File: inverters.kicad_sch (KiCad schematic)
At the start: 10 parts, among them U13 74LVC1G04, U14 74LVC1G04, U15 74LVC1G04

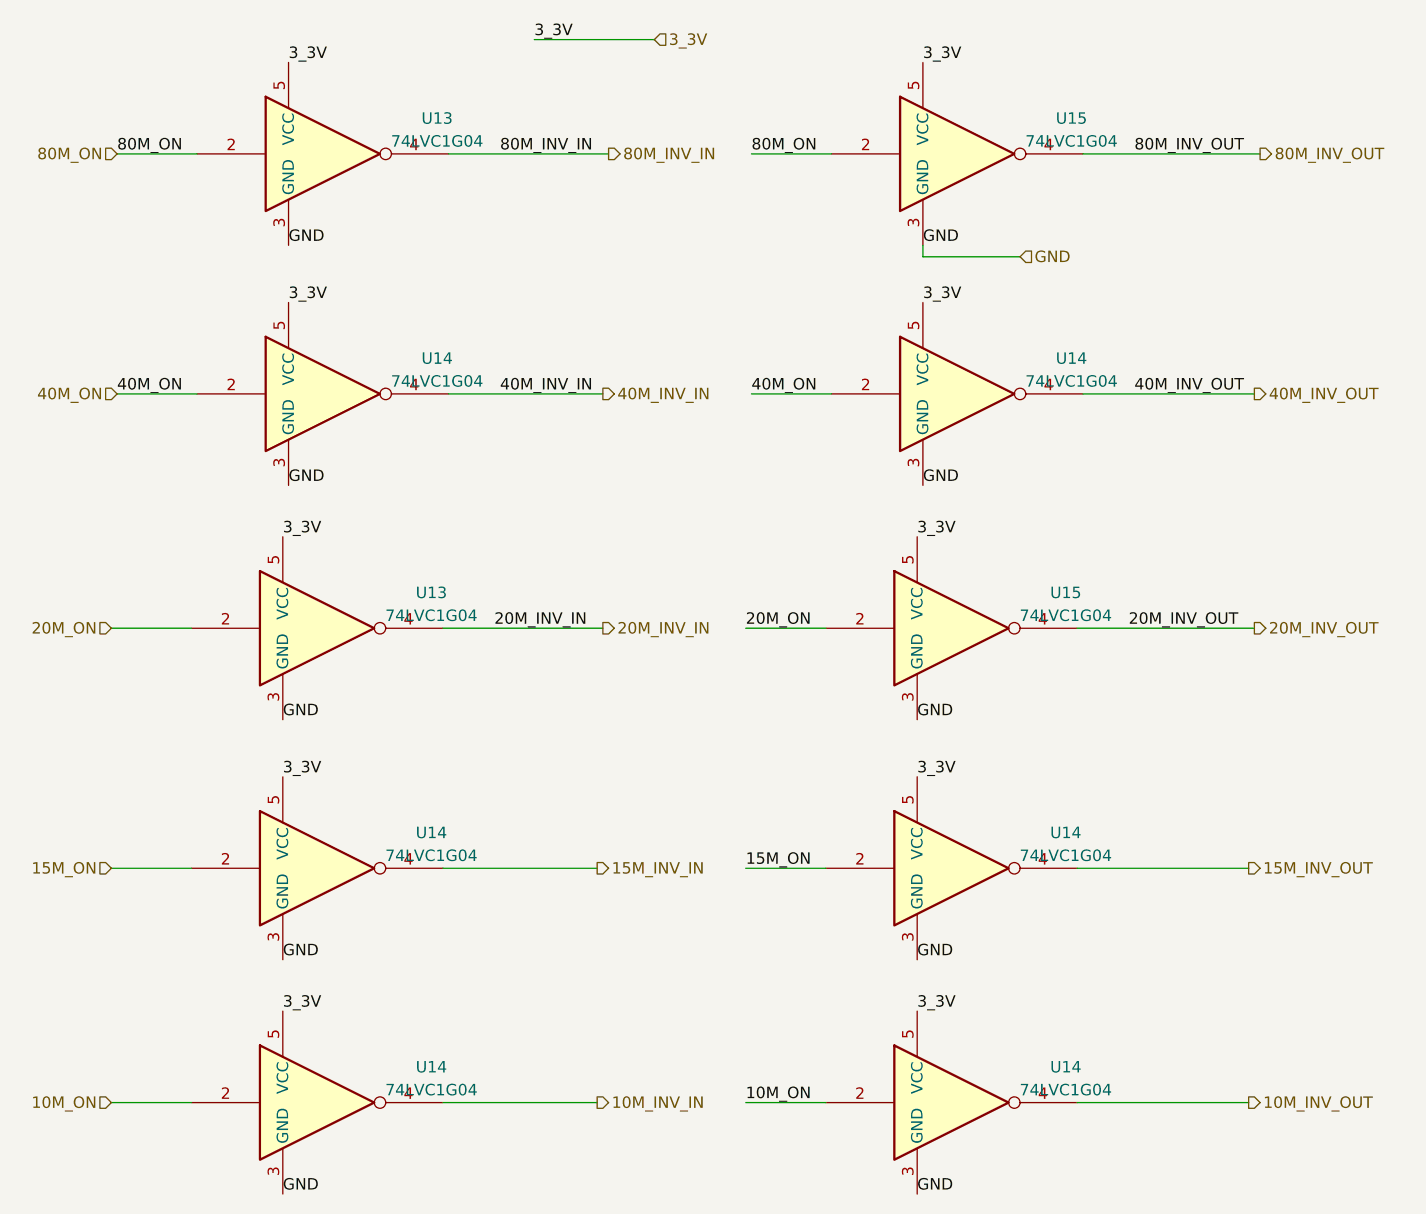
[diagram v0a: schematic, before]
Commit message: Fixed logic gate, is now NOR.  Cleaned up layout.
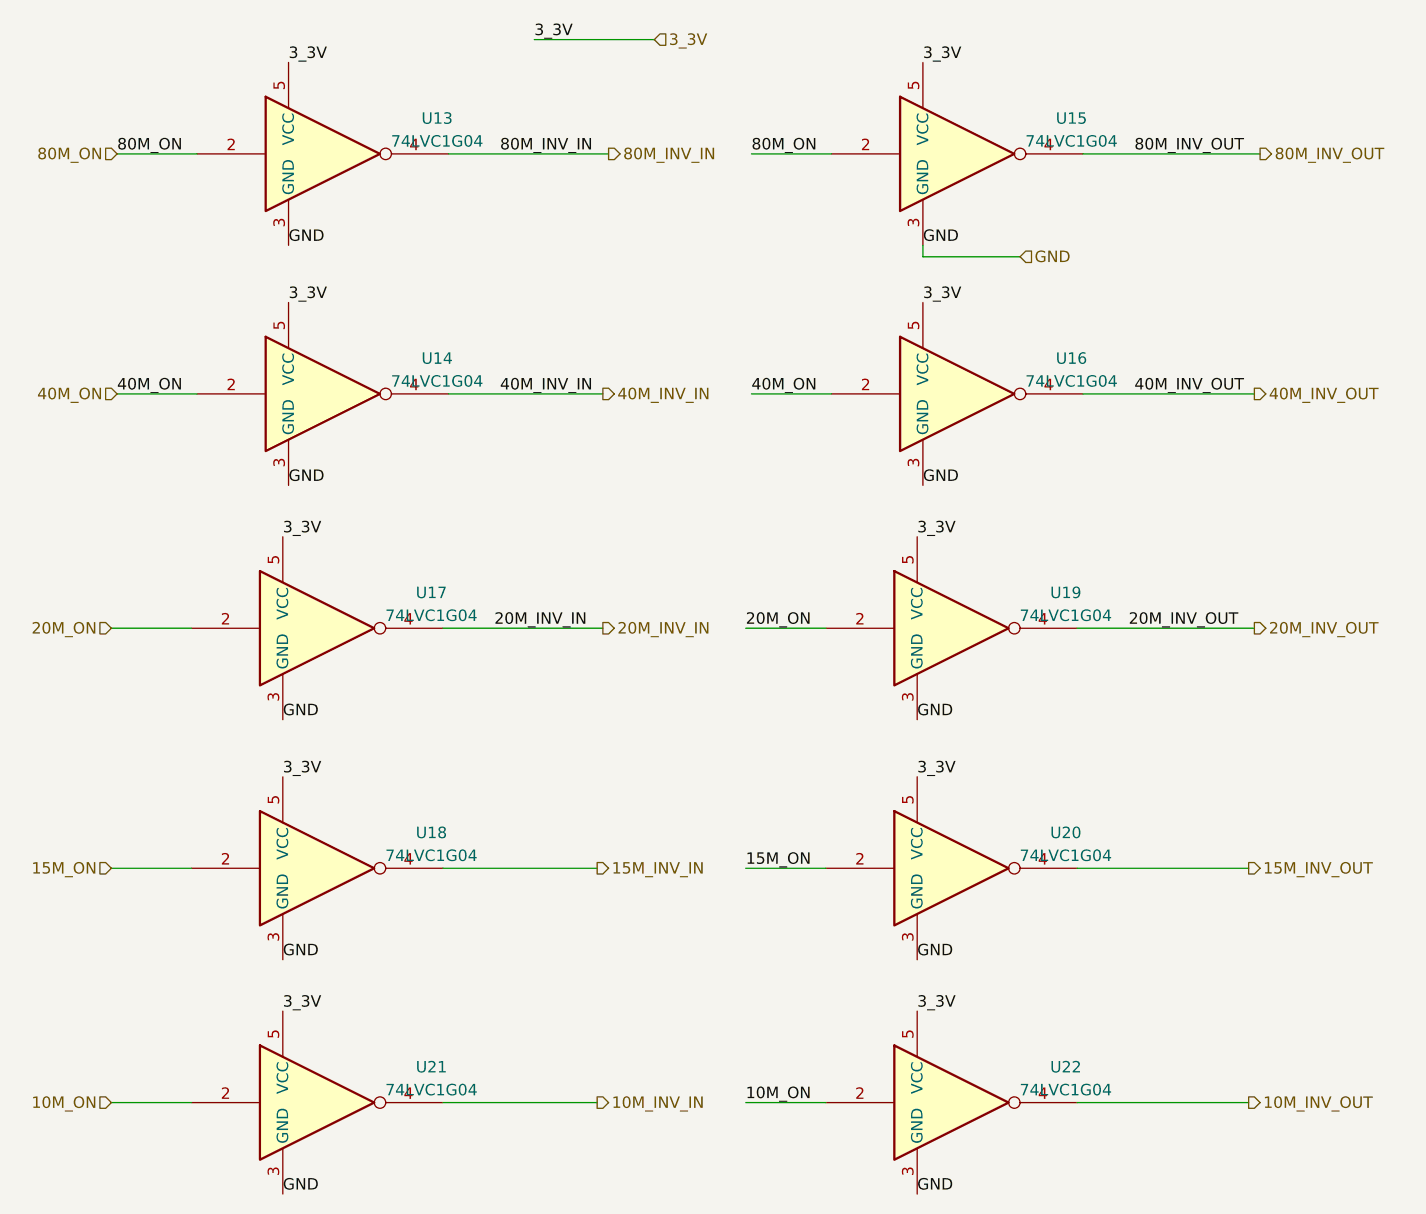
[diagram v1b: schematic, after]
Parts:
- renumbered U14 to U16, U13 to U17, U14 to U18, U15 to U19, U14 to U20, U14 to U21, U14 to U22
